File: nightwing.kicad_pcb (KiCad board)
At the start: 2 copper layers, 165.4 x 129.6 mm, 142 parts, among them J1 USB_C_Receptacle_USB2.0, J2 USB_C_Receptacle_USB2.0, J3 OLED, SW1 SW_PUSH, SW10 SW_PUSH, SW11 SW_PUSH, SW12 SW_PUSH, SW13 SW_PUSH, SW14 SW_PUSH, SW15 SW_PUSH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

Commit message: nightwing pre nick
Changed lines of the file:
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@@
     (visible_elements FFFFFF7F)
     (pcbplotparams
-      (layerselection 0x3dc3c_ffffffff)
+      (layerselection 0x3dc30_ffffffff)
       (usegerberextensions false)
       (usegerberattributes true)
@@
       (drillshape 0)
       (scaleselection 1)
-      (outputdirectory "./"))
+      (outputdirectory "pos/"))
   )
   (net 0 "")
@@
       (effects (font (size 0.5 0.5) (thickness 0.08)))
     )
-    (pad 1 smd roundrect (at -0.9125 0 90) (size 1.025 1.4) (layers F.Cu F.Paste F.Mask) (roundrect_rratio 0.2439014634146341)
+    (pad 1 smd roundrect (at -0.9125 0 90) (size 1.025 1.4) (layers F.Cu F.Paste F.Mask) (roundrect_rratio 0.2439004878048781)
       (net 88 "Net-(R6-Pad1)"))
-    (pad 2 smd roundrect (at 0.9125 0 90) (size 1.025 1.4) (layers F.Cu F.Paste F.Mask) (roundrect_rratio 0.2439014634146341)
+    (pad 2 smd roundrect (at 0.9125 0 90) (size 1.025 1.4) (layers F.Cu F.Paste F.Mask) (roundrect_rratio 0.2439004878048781)
       (net 92 "Net-(D27-Pad1)"))
     (model ${KISYS3DMOD}/Resistor_SMD.3dshapes/R_0805_2012Metric.wrl
@@
       (effects (font (size 0.5 0.5) (thickness 0.08)))
     )
-    (pad 1 smd roundrect (at -0.9125 0 90) (size 1.025 1.4) (layers F.Cu F.Paste F.Mask) (roundrect_rratio 0.2439014634146341)
+    (pad 1 smd roundrect (at -0.9125 0 90) (size 1.025 1.4) (layers F.Cu F.Paste F.Mask) (roundrect_rratio 0.2439004878048781)
       (net 89 "Net-(R8-Pad1)"))
-    (pad 2 smd roundrect (at 0.9125 0 90) (size 1.025 1.4) (layers F.Cu F.Paste F.Mask) (roundrect_rratio 0.2439014634146341)
+    (pad 2 smd roundrect (at 0.9125 0 90) (size 1.025 1.4) (layers F.Cu F.Paste F.Mask) (roundrect_rratio 0.2439004878048781)
       (net 90 "Net-(D26-Pad1)"))
     (model ${KISYS3DMOD}/Resistor_SMD.3dshapes/R_0805_2012Metric.wrl
@@
       (effects (font (size 0.5 0.5) (thickness 0.08)))
     )
-    (pad 2 smd roundrect (at 0.9125 0 90) (size 1.025 1.4) (layers F.Cu F.Paste F.Mask) (roundrect_rratio 0.2439014634146341)
+    (pad 2 smd roundrect (at 0.9125 0 90) (size 1.025 1.4) (layers F.Cu F.Paste F.Mask) (roundrect_rratio 0.2439004878048781)
       (net 4 "Net-(J1-PadB5)"))
-    (pad 1 smd roundrect (at -0.9125 0 90) (size 1.025 1.4) (layers F.Cu F.Paste F.Mask) (roundrect_rratio 0.2439014634146341)
+    (pad 1 smd roundrect (at -0.9125 0 90) (size 1.025 1.4) (layers F.Cu F.Paste F.Mask) (roundrect_rratio 0.2439004878048781)
       (net 91 GND))
     (model ${KISYS3DMOD}/Resistor_SMD.3dshapes/R_0805_2012Metric.wrl
@@
       (effects (font (size 0.5 0.5) (thickness 0.08)))
     )
-    (pad 1 smd roundrect (at -0.9125 0 90) (size 1.025 1.4) (layers F.Cu F.Paste F.Mask) (roundrect_rratio 0.2439014634146341)
+    (pad 1 smd roundrect (at -0.9125 0 90) (size 1.025 1.4) (layers F.Cu F.Paste F.Mask) (roundrect_rratio 0.2439004878048781)
       (net 91 GND))
-    (pad 2 smd roundrect (at 0.9125 0 90) (size 1.025 1.4) (layers F.Cu F.Paste F.Mask) (roundrect_rratio 0.2439014634146341)
+    (pad 2 smd roundrect (at 0.9125 0 90) (size 1.025 1.4) (layers F.Cu F.Paste F.Mask) (roundrect_rratio 0.2439004878048781)
       (net 1 "Net-(J1-PadA5)"))
     (model ${KISYS3DMOD}/Resistor_SMD.3dshapes/R_0805_2012Metric.wrl
@@
       (effects (font (size 0.5 0.5) (thickness 0.08)))
     )
-    (pad 1 smd roundrect (at -0.9125 0 180) (size 1.025 1.4) (layers F.Cu F.Paste F.Mask) (roundrect_rratio 0.2439014634146341)
+    (pad 1 smd roundrect (at -0.9125 0 180) (size 1.025 1.4) (layers F.Cu F.Paste F.Mask) (roundrect_rratio 0.2439004878048781)
       (net 70 D+))
-    (pad 2 smd roundrect (at 0.9125 0 180) (size 1.025 1.4) (layers F.Cu F.Paste F.Mask) (roundrect_rratio 0.2439014634146341)
+    (pad 2 smd roundrect (at 0.9125 0 180) (size 1.025 1.4) (layers F.Cu F.Paste F.Mask) (roundrect_rratio 0.2439004878048781)
       (net 2 "Net-(J1-PadA6)"))
     (model ${KISYS3DMOD}/Resistor_SMD.3dshapes/R_0805_2012Metric.wrl
@@
       (effects (font (size 0.5 0.5) (thickness 0.08)))
     )
-    (pad 1 smd roundrect (at -0.9125 0 180) (size 1.025 1.4) (layers F.Cu F.Paste F.Mask) (roundrect_rratio 0.2439014634146341)
+    (pad 1 smd roundrect (at -0.9125 0 180) (size 1.025 1.4) (layers F.Cu F.Paste F.Mask) (roundrect_rratio 0.2439004878048781)
       (net 69 D-))
-    (pad 2 smd roundrect (at 0.9125 0 180) (size 1.025 1.4) (layers F.Cu F.Paste F.Mask) (roundrect_rratio 0.2439014634146341)
+    (pad 2 smd roundrect (at 0.9125 0 180) (size 1.025 1.4) (layers F.Cu F.Paste F.Mask) (roundrect_rratio 0.2439004878048781)
       (net 3 "Net-(J1-PadA7)"))
     (model ${KISYS3DMOD}/Resistor_SMD.3dshapes/R_0805_2012Metric.wrl
@@
       (effects (font (size 0.5 0.5) (thickness 0.08)))
     )
-    (pad 1 smd roundrect (at -0.9125 0) (size 1.025 1.4) (layers F.Cu F.Paste F.Mask) (roundrect_rratio 0.2439014634146341)
+    (pad 1 smd roundrect (at -0.9125 0) (size 1.025 1.4) (layers F.Cu F.Paste F.Mask) (roundrect_rratio 0.2439004878048781)
       (net 35 VCC))
-    (pad 2 smd roundrect (at 0.9125 0) (size 1.025 1.4) (layers F.Cu F.Paste F.Mask) (roundrect_rratio 0.2439014634146341)
+    (pad 2 smd roundrect (at 0.9125 0) (size 1.025 1.4) (layers F.Cu F.Paste F.Mask) (roundrect_rratio 0.2439004878048781)
       (net 66 RESET))
     (model ${KISYS3DMOD}/Resistor_SMD.3dshapes/R_0805_2012Metric.wrl
@@
       (effects (font (size 0.5 0.5) (thickness 0.08)))
     )
-    (pad 1 smd roundrect (at -0.9125 0 90) (size 1.025 1.4) (layers F.Cu F.Paste F.Mask) (roundrect_rratio 0.2439014634146341)
+    (pad 1 smd roundrect (at -0.9125 0 90) (size 1.025 1.4) (layers F.Cu F.Paste F.Mask) (roundrect_rratio 0.2439004878048781)
       (net 35 VCC))
-    (pad 2 smd roundrect (at 0.9125 0 90) (size 1.025 1.4) (layers F.Cu F.Paste F.Mask) (roundrect_rratio 0.2439014634146341)
+    (pad 2 smd roundrect (at 0.9125 0 90) (size 1.025 1.4) (layers F.Cu F.Paste F.Mask) (roundrect_rratio 0.2439004878048781)
       (net 85 "Net-(R1-Pad2)"))
     (model ${KISYS3DMOD}/Resistor_SMD.3dshapes/R_0805_2012Metric.wrl
@@
     )
   )
+  (gr_line (start 49.75 105) (end 49.75 93.95) (layer Edge.Cuts) (width 0.05))
   (gr_text "nightwing rev1.0\n" (at 134.99856 82.967865) (layer F.SilkS)
     (effects (font (size 1.5 1.5) (thickness 0.15)) (justify left))
@@
   (gr_line (start 108 105) (end 49.75 105) (layer Edge.Cuts) (width 0.1))
   (gr_line (start 108 123.27) (end 108 105) (layer Edge.Cuts) (width 0.1))
-  (gr_line (start 49.75 105) (end 49.75 93.95) (layer Edge.Cuts) (width 0.05))
   (gr_line (start 49.75 93.95) (end 11.66 93.95) (layer Edge.Cuts) (width 0.05))
   (gr_line (start 19.71 15.65) (end 19.71 10.18) (layer Margin) (width 0.15))

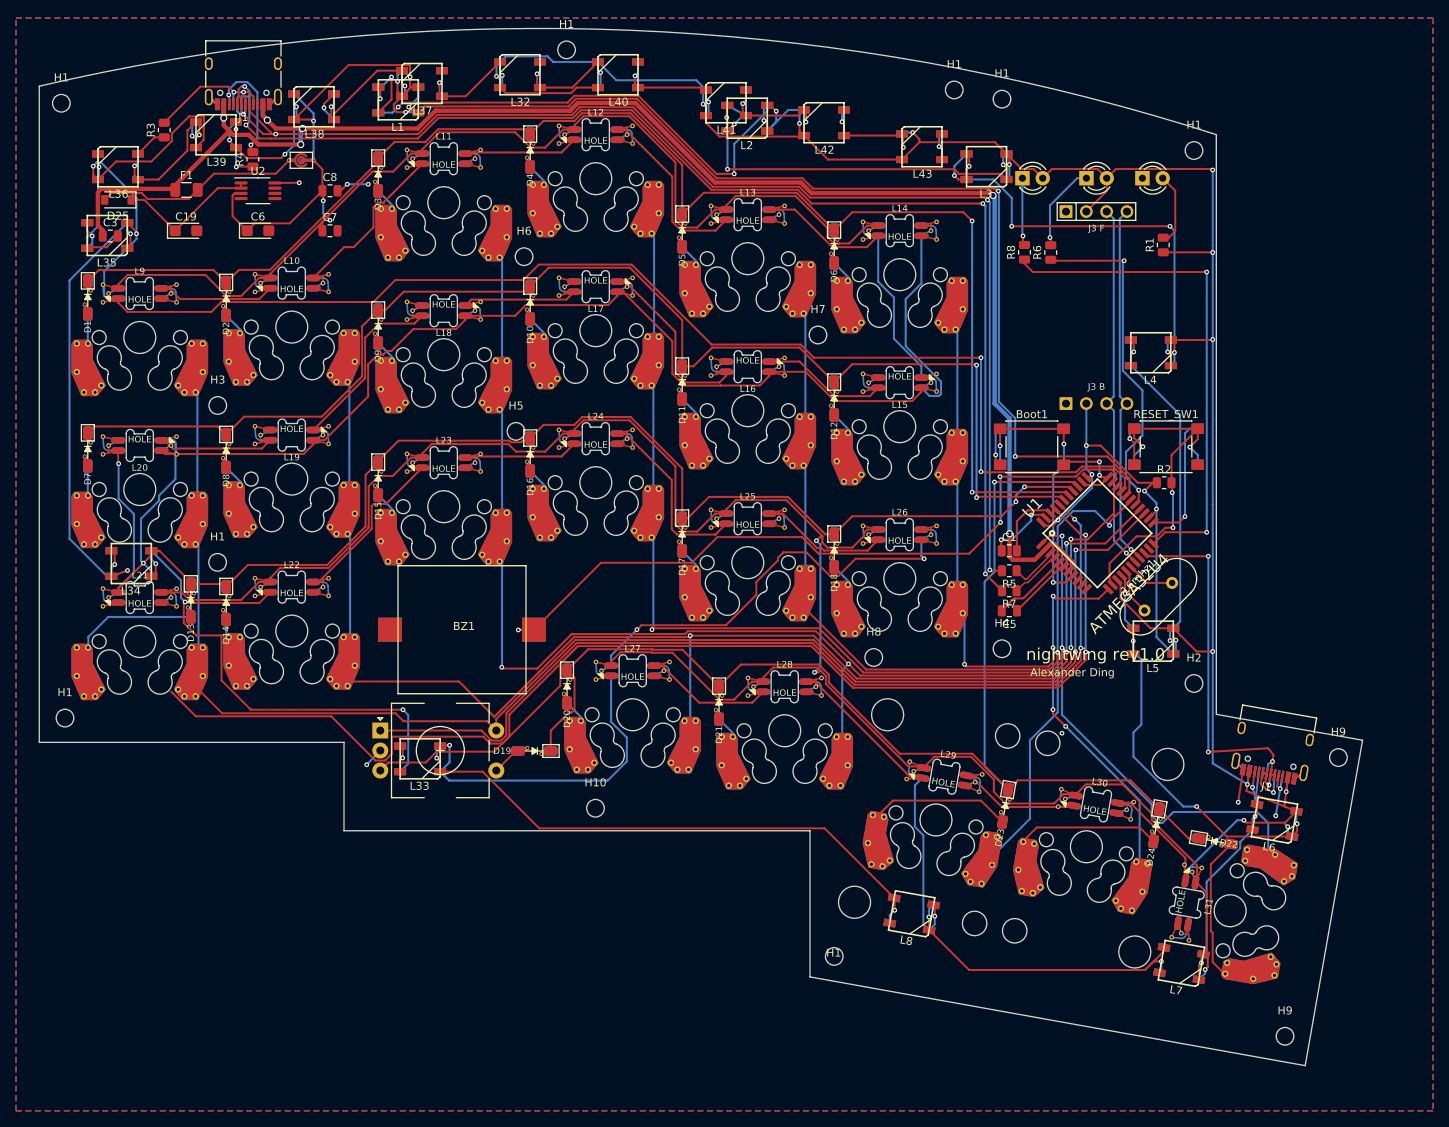
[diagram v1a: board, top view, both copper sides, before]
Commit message: fixed drc check
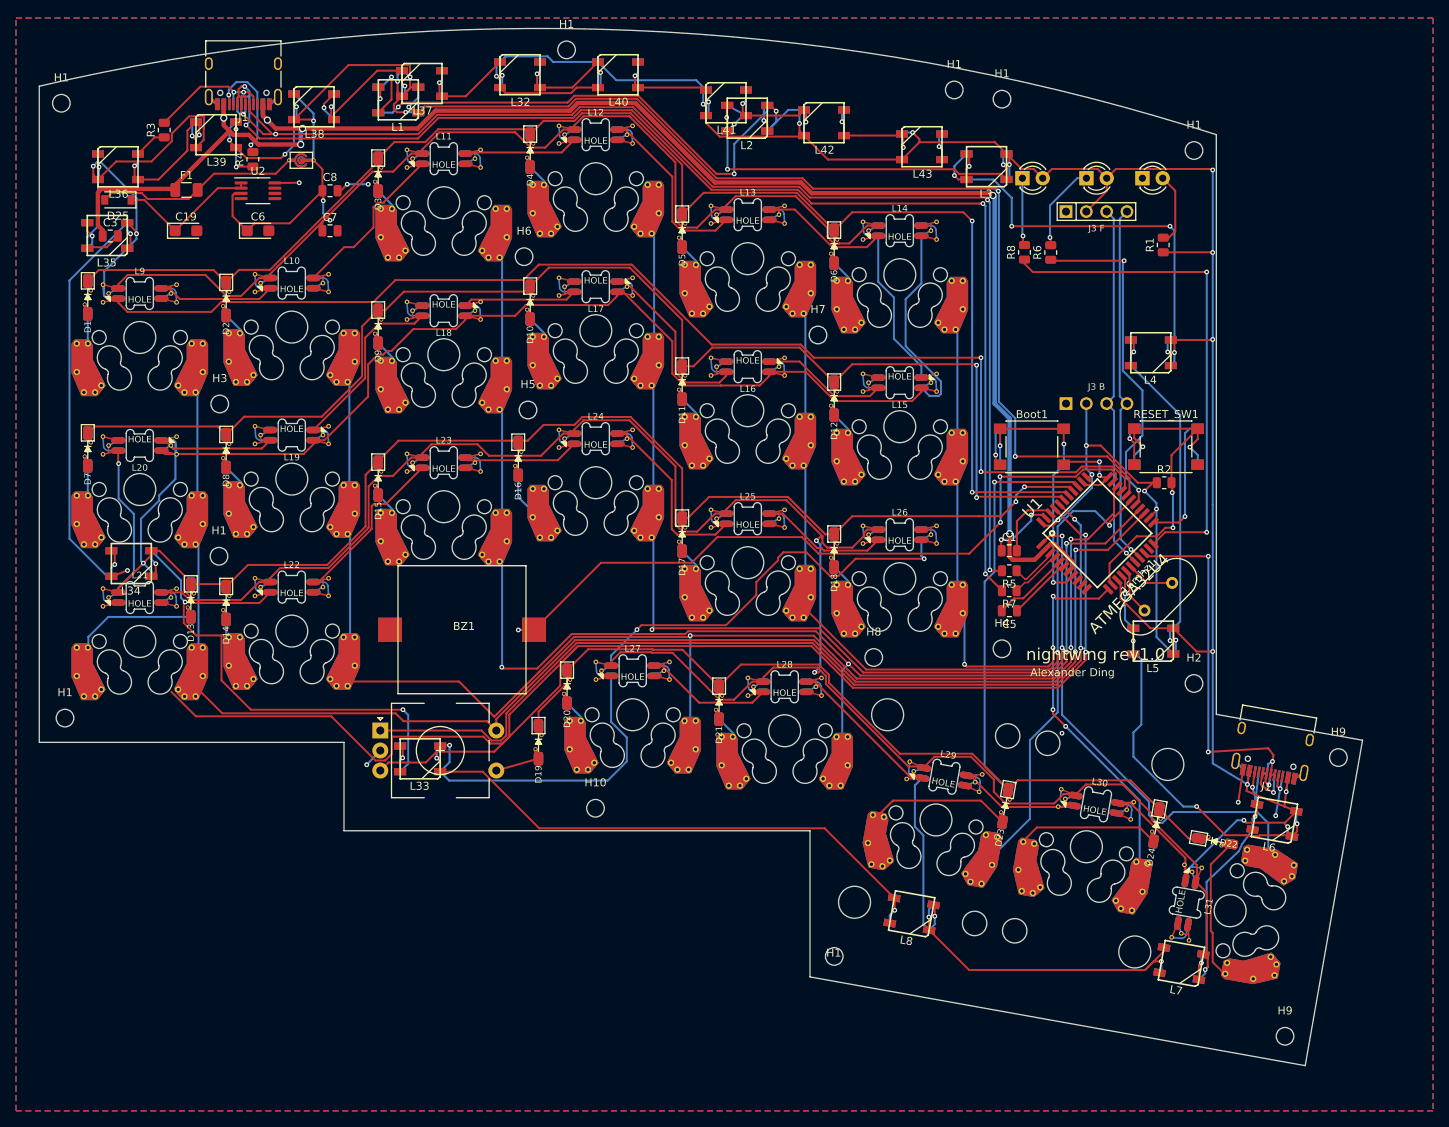
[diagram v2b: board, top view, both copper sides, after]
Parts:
- moved H5 3.07 mm to (72.7, 52.4)
- moved D16 1.58 mm to (71.5, 58.5)
- moved D19 1.21 mm to (74.1, 93.9), turned to 270 degrees
- moved H1 0.78 mm to (34.1, 70.7)
- moved H3 0.31 mm to (34.2, 51.7)
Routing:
- net A0: track 156.4 -> 152.5 mm
- net Net-(D19-Pad2): track 3.71 -> 5.48 mm

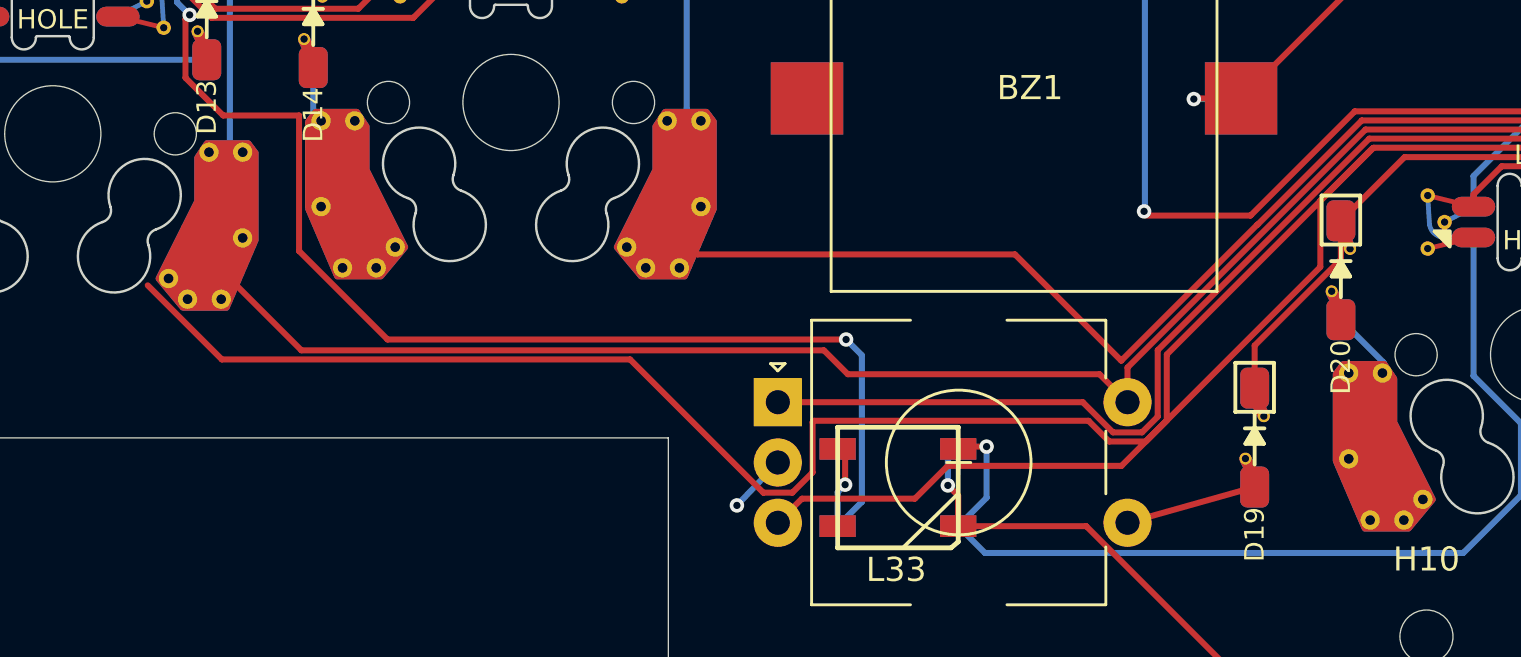
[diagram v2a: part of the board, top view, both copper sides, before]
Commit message: fixed dangling trace a5
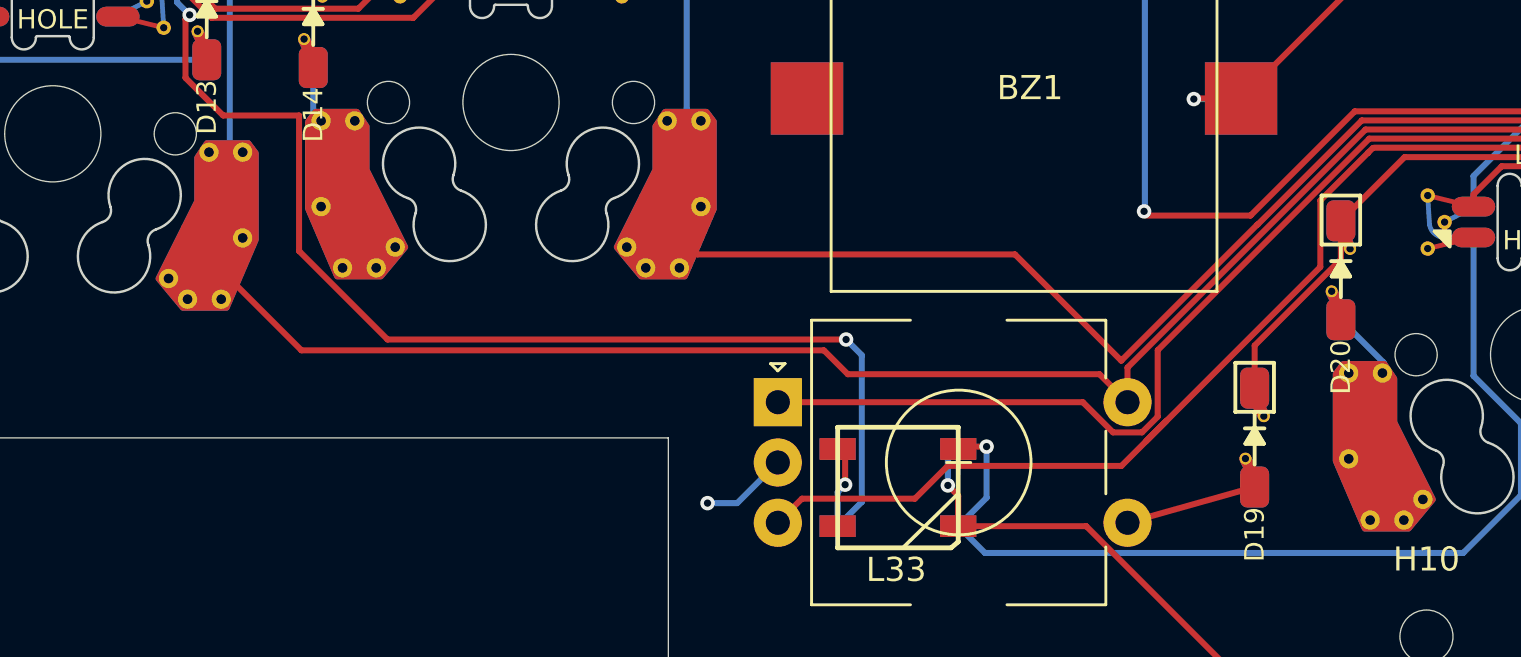
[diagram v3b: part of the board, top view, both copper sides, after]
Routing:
- net A5: track 184.5 -> 121.8 mm
- net GND: track 142.5 -> 143.7 mm
